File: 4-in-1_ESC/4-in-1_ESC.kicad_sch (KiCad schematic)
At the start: 37 parts, among them CN1 SM10B-SRSS-TB, CN2 SM07B-SRSS-TB, J1 BLDC Solder Pads, J2 BLDC Solder Pads, J3 BLDC Solder Pads, J4 BLDC Solder Pads, U1 INA181A2IDBVR

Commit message: update
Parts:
- added H4, H5, H6, H7: MountingHole_Pad, MountingHole:MountingHole_3.2mm_M3_DIN965_Pad_TopBottom, symbol Mechanical:MountingHole_Pad
- C66, C82, C86: footprint Capacitor_SMD:C_0402_1005Metric -> Capacitor_SMD:C_0201_0603Metric
- J1, J2, J3, J4: footprint (none) -> easyeda_import:3_Phase_Solder_Pads
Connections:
- net GND_BAT is gone; now on net GND: C1.2, C10.2, C11.2, C12.2, C13.2, C14.2, C15.2, C16.2, C17.2, C18.2, C19.2, C2.2, C20.2, C21.2, C22.2, C23.2, C24.2, C3.2, C4.2, C5.2, C6.2, C7.2, C8.2, C9.2
- net GND: now also H4.1, H5.1, H6.1, H7.1
- no-connect marks 0 -> 3
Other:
- sheet STM32F051K8U6 ports: added CURRENT_SENSE, KISS_TELEM; removed none
- sheet STM32F051K8U7 ports: added CURRENT_SENSE, KISS_TELEM; removed none
- sheet STM32F051K8U9 ports: added CURRENT_SENSE, KISS_TELEM; removed none

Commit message: changes
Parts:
- removed H2: VBAT- PAD, symbol Mechanical:MountingHole_Pad
- removed H3: VBAT+ PAD, symbol Mechanical:MountingHole_Pad
- added J5: (no value), easyeda_import:VBAT_SOLDER_PADS, symbol easyeda_import:VBAT_Solder_Pads
- added R116, R117, R118, R119, R120: 470R, Resistor_SMD:R_0201_0603Metric, symbol Device:R_Small_US
- H4, H5, H6, H7: footprint MountingHole:MountingHole_3.2mm_M3_DIN965_Pad_TopBottom -> easyeda_import:MountingHole_3.2mm_Custom
- J1, J2: footprint easyeda_import:3_Phase_Solder_Pads -> easyeda_import:3_Phase_Solder_Pads_Left
- J3, J4: footprint easyeda_import:3_Phase_Solder_Pads -> easyeda_import:3_Phase_Solder_Pads_Right
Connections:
- net DSHOT_M1: now also R116.1; no longer CN2.3
- net DSHOT_M2: now also R117.1; no longer CN2.4
- net DSHOT_M3: now also R118.1; no longer CN2.5
- net DSHOT_M4: now also R119.1; no longer CN2.6
- net GND: now also J5.2 (-)
- net KISS_TELEM: now also R120.2; no longer CN2.2
- net VBAT: now also J5.1 (+)
- new net: CN2.2, R120.1
- new net: CN2.3, R116.2
- new net: CN2.4, R117.2
- new net: CN2.5, R118.2
- new net: CN2.6, R119.2

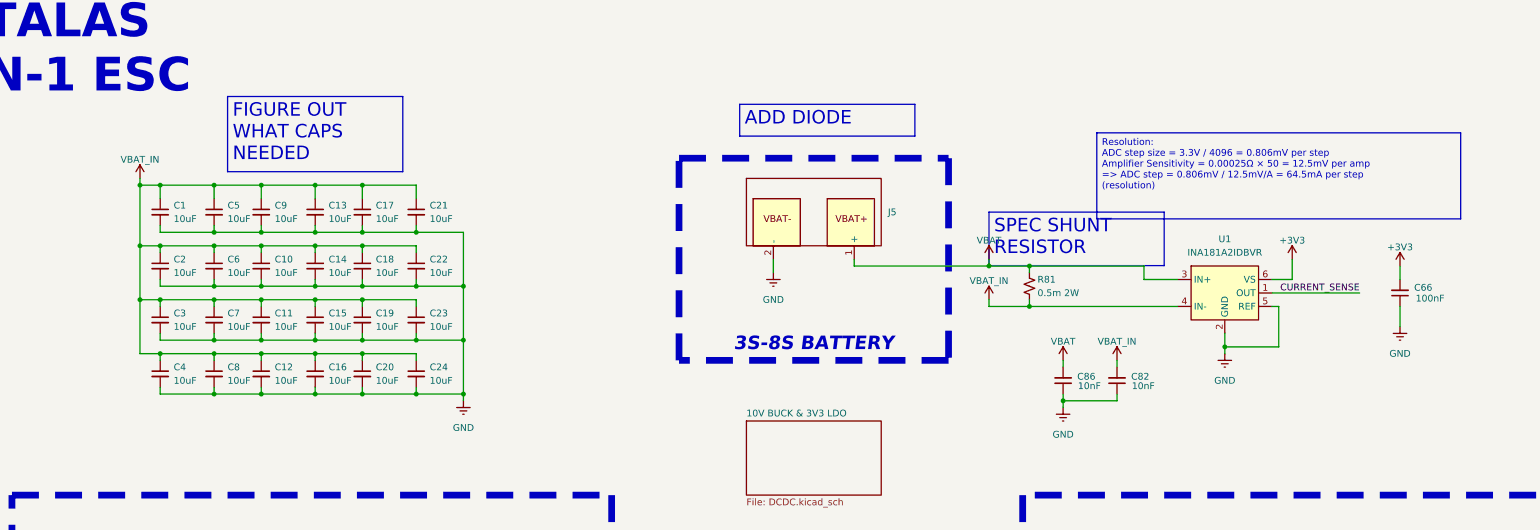
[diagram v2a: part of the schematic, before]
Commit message: Schematic Updates
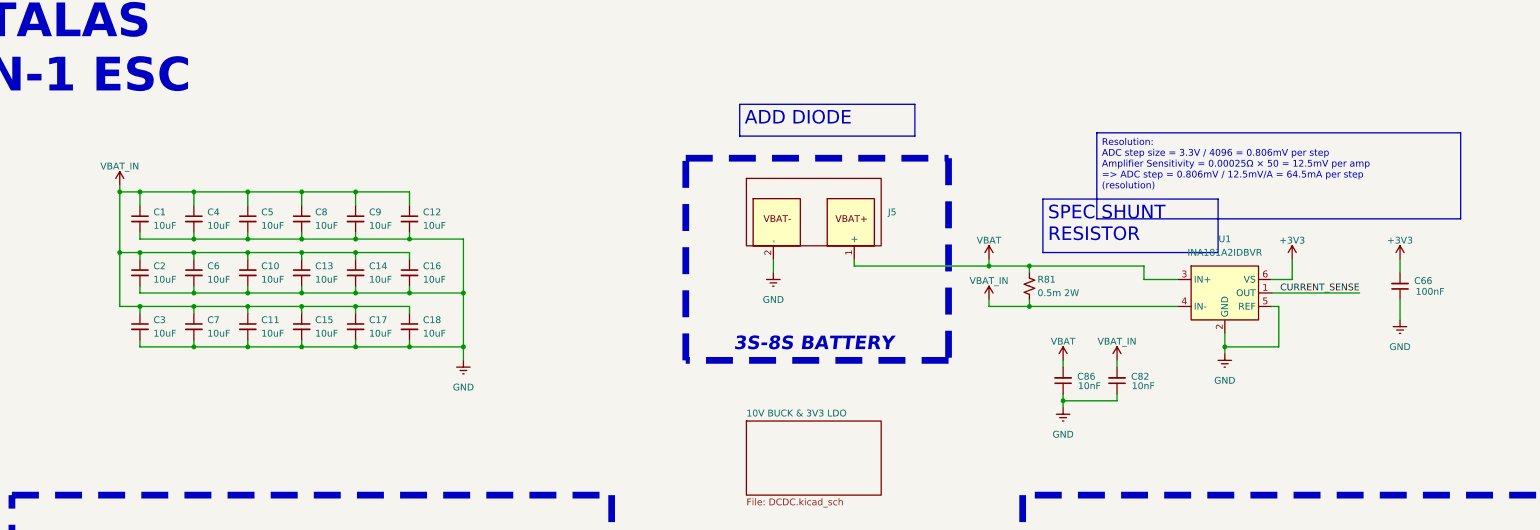
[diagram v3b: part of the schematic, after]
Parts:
- removed C19, C20, C21, C22, C23, C24: 10uF, Capacitor_SMD:C_0805_2012Metric, symbol Device:C_Small
- C1, C10, C11, C12, C13, C14, C15, C16, C17, C18, C2, C3, C4, C5, C6, C7, C8, C9: LCSC_Part_Number (none) -> C22367838
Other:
- moved on the sheet: C1, C66

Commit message: UPDATE
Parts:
- removed C66: 100nF, Capacitor_SMD:C_0201_0603Metric, symbol Device:C_Small
- removed C82, C86: 10nF, Capacitor_SMD:C_0201_0603Metric, symbol Device:C_Small
- removed R81: 0.5m 2W, symbol Device:R_Small_US
- removed U1: INA181A2IDBVR, easyeda_import:SOT-23-6_L2.9-W1.6-P0.95-LS2.8-BL, symbol easyeda_import:INA181A2IDBVR
- added D17: SMAJ40A, Diode_SMD:D_SMA, symbol Diode:SMAJ40A
- added R1, R3, R4, R5, R6, R7: 0.5m, symbol Device:R_Small_US
- added U1: OPA333AIDBVR, easyeda_import:SOT-23-5_L2.9-W1.6-P0.95-LS2.8-BR, symbol easyeda_import:OPA333AIDBVR
- C1, C10, C11, C12, C13, C14, C15, C16, C17, C18, C2, C3, C4, C5, C6, C7, C8, C9: Voltage Rating (none) -> 100V
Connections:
- net VBAT is gone; now on net VBAT_IN: J5.1 (+)
- net CURRENT_SENSE: now also R5.1, U1.1 (OUT)
- net GND: now also D17.1 (A1), R1.2, R4.1, R6.1, U1.2 (V-); no longer J5.2 (-)
- net VBAT_IN: now also D17.2 (A2)
- new net: R3.1, R5.2, U1.4 (-IN)
- new net: J5.2 (-), R1.1, R3.2
- new net: R4.2, R6.2, U1.3 (+IN)
- new net +10V: U1.5 (V+)

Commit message: update
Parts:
- removed C1, C10, C11, C12, C13, C14, C15, C17, C18, C2, C3, C4, C5, C6, C7, C8, C9: 10uF, Capacitor_SMD:C_0805_2012Metric, symbol Device:C_Small
- removed R1, R3, R4, R5, R6: 0.5m, symbol Device:R_Small_US
- removed U1: OPA333AIDBVR, easyeda_import:SOT-23-5_L2.9-W1.6-P0.95-LS2.8-BR, symbol easyeda_import:OPA333AIDBVR
- added C19, C20, C21, C22, C23, C24, C25, C66, C92, C93, C94: 10uF, Capacitor_SMD:C_1210_3225Metric, symbol Device:C_Small
- added C82, C86, C91: 100nF, Capacitor_SMD:C_0201_0603Metric, symbol Device:C_Small
- added NT1: NetTie_2, NetTie:NetTie-2_SMD_Pad2.0mm, symbol Device:NetTie_2
- added R1: 0.2m 6W SHUNT, easyeda_import:RES-SMD_L6.3-W3.1-1, symbol easyeda_import:ASR-M-3-0.25F
- added R10: 1k, symbol Device:R_Small_US
- added R121: 10k, Resistor_SMD:R_0201_0603Metric, symbol Device:R_Small_US
- added R9: 10k, symbol Device:R_Small_US
- added U1: INA180A2IDBVR, easyeda_import:SOT-23-5_L3.0-W1.7-P0.95-LS2.8-BL, symbol easyeda_import:INA180A2IDBVR
- C16: footprint Capacitor_SMD:C_0805_2012Metric -> Capacitor_SMD:C_1210_3225Metric
- R7: value 0.5m -> 100k
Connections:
- net +3V3: now also C82.1, R121.2, U1.5 (VS)
- net CURRENT_SENSE: now also C86.1, R10.1
- net GND: now also C19.2, C20.2, C21.2, C22.2, C23.2, C24.2, C25.2, C66.2, C82.2, C86.2, C91.2, C92.2, C93.2, C94.2, NT1.1, R1.1, R9.1, U1.2 (GND)
- net KISS_TELEM: now also R121.1
- net VBAT_IN: now also R7.2, C19.1, C20.1, C21.1, C22.1, C23.1, C24.1, C25.1, C66.1, C92.1, C93.1, C94.1
- net at J5.2 (-): now also R1.2, U1.4 (IN-)
- net VBAT_SENSE: now reaches R7.1
- net VBAT_SENSE: now also C91.1, R9.2
- new net: R10.2, U1.1 (OUT)
- new net: NT1.2, U1.3 (IN+)
- no-connect marks 3 -> 6
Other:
- sheet STM32F051K8U6 ports: added VBAT_SENSE; removed none
- sheet STM32F051K8U7 ports: added VBAT_SENSE; removed none
- sheet STM32F051K8U8 ports: added VBAT_SENSE; removed none
- sheet STM32F051K8U9 ports: added VBAT_SENSE; removed none
- note added: "3S-8S | AM32 | OPEN SOURCE"
- note added: "By: Jun Young Kim"
- note added: "INPUT CAPACITORS"
- note added: "LOW SIDE CURRENT SENSING"
- note added: "REV 1"
- note added: "VBAT VOLTAGE DIVIDER"
- note removed: "3S-8S"
- moved on the sheet: C16, H4, H5, H6, H7, R120, R7
